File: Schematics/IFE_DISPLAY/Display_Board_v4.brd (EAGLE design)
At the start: 96.5 x 83.8 mm, 38 parts, among them J1 POWER_JACKPTH

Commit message: Display v4 - Routing
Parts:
- added R11, R4, R6: 23k, rcl:R0603
- added U$12: MC34063AD, Display_Custom:SMC
- J1: value POWER_JACKPTH -> 5.5x2.1mm Barrel; device SparkFun-Connectors:POWER_JACK_PTH -> SparkFun-Connectors:POWER_JACK_SMD
- moved J1 72.1 mm to (3.35, 68.6)
- moved U$7 33.0 mm to (8.89, 14.0)
- moved U$9 33.0 mm to (41.9, 14.0)
- moved R2 28.6 mm to (71.1, 60.9), turned to 180 degrees
- moved R3 28.6 mm to (71.1, 63.4), turned to 180 degrees
- moved C1 23.4 mm to (77.5, 61.0), turned to 90 degrees
- moved C2 20.1 mm to (64.8, 62.2), turned to 270 degrees
- moved U$11 18.2 mm to (59.7, 74.9), turned to 270 degrees
- moved U$10 15.3 mm to (73.7, 73.7), turned to 0 degrees
- moved R8 9.75 mm to (72.5, 40.6), turned to 90 degrees
- moved R9 9.68 mm to (72.3, 50.8), turned to 270 degrees
- moved C8 9.64 mm to (74.9, 40.6)
- moved C9 9.57 mm to (74.9, 50.8), turned to 270 degrees
- moved FUSE 9.16 mm to (85.1, 71.1), flipped to the bottom, turned to 90 degrees
- moved U$6 1.80 mm to (55.9, 49.5)
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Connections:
- net ~CS_CAN renamed !CS_CAN
- net ~INT_CAN renamed !INT_CAN
- new net !A_CS: ATMEGA328P.9, U$7.9
- new net !B_CS: ATMEGA328P.2, U$8.9
- new net !C_CS: ATMEGA328P.1, U$9.9
- new net A_0: U$1.12, U$7.3
- new net A_1: U$1.9, U$7.8
- new net A_2: U$1.8, U$7.5
- new net A_3: U$1.6, U$7.6
- new net A_A: U$1.11, U$7.11
- new net A_B: U$1.7, U$7.13
- new net A_C: U$1.4, U$7.17
- new net A_D: U$1.2, U$7.20
- new net A_DP: U$1.3, U$7.19
- new net A_E: U$1.1, U$7.18
- new net A_F: U$1.10, U$7.12
- new net A_G: U$1.5, U$7.14
- new net B_0: U$5.12, U$8.3
- new net B_1: U$5.9, U$8.8
- new net B_2: U$5.8, U$8.5
- new net B_3: U$5.6, U$8.6
- new net B_A: U$5.11, U$8.11
- new net B_B: U$5.7, U$8.13
- new net B_C: U$5.4, U$8.17
- new net B_D: U$5.2, U$8.20
- new net B_DP: U$5.3, U$8.19
- new net B_E: U$5.1, U$8.18
- new net B_F: U$5.10, U$8.12
- new net B_G: U$5.5, U$8.14
- new net C_0: U$6.12, U$9.3
- new net C_1: U$6.9, U$9.8
- new net C_2: U$6.8, U$9.5
- new net C_3: U$6.6, U$9.6
- new net C_A: U$6.11, U$9.11
- new net C_B: U$6.7, U$9.13
- new net C_C: U$6.4, U$9.17
- new net C_D: U$6.2, U$9.20
- new net C_DP: U$6.3, U$9.19
- new net C_E: U$6.1, U$9.18
- new net C_F: U$6.10, U$9.12
- new net C_G: U$6.5, U$9.14
- new net N$15: R6.1, U$8.15
- new net N$19: R11.1, U$9.15
- new net N$22: R4.1, U$7.15
- net +5V: now also R11.2, R4.2, R6.2, U$7.16, U$8.16, U$9.16
- net GND: now also J1.P$4, U$12.A, U$7.4, U$7.7, U$8.4, U$8.7, U$9.4, U$9.7; no longer J1.GNDBREAK
- net MISO: now also U$7.1, U$8.1, U$9.1
- net MOSI: now also U$7.2, U$8.2, U$9.2
- net N$8: now also U$12.C
- net PWR_IN_12: now also J1.VIN0; no longer J1.PWR
- net SCK: now also U$7.10, U$8.10, U$9.10
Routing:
- net PWR_IN_12: track 0.00 -> 134.3 mm
- net MISO: track 0.00 -> 61.8 mm, vias 0 -> 4
- net MOSI: track 0.00 -> 61.6 mm, vias 0 -> 4
- net CANL: track 0.00 -> 59.2 mm
- net CANH: track 0.00 -> 58.8 mm, vias 0 -> 1
- net GND: track 0.00 -> 52.2 mm
- net N$8: track 0.00 -> 39.7 mm
- net +5V: track 0.00 -> 35.6 mm, vias 0 -> 1
- net V+: track 0.00 -> 13.8 mm
- net 2515_OSC2: track 0.00 -> 12.3 mm
- net XTAL1: track 0.00 -> 11.5 mm
- net LED2: track 0.00 -> 9.45 mm
- net TXCAN: track 0.00 -> 8.70 mm
- net RESET: track 0.00 -> 8.25 mm
- net 2515_OSC1: track 0.00 -> 7.77 mm
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
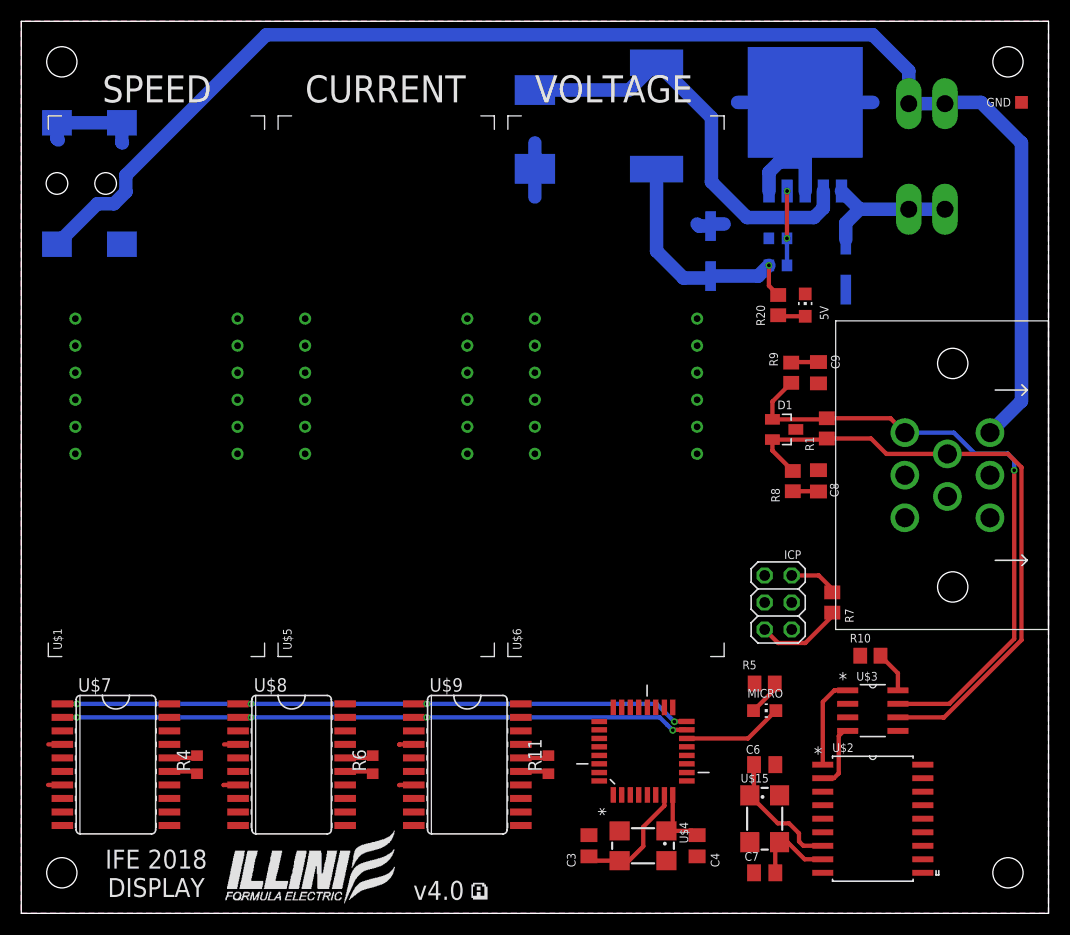
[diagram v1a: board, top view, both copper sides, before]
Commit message: Display v4 - ready to autoroute
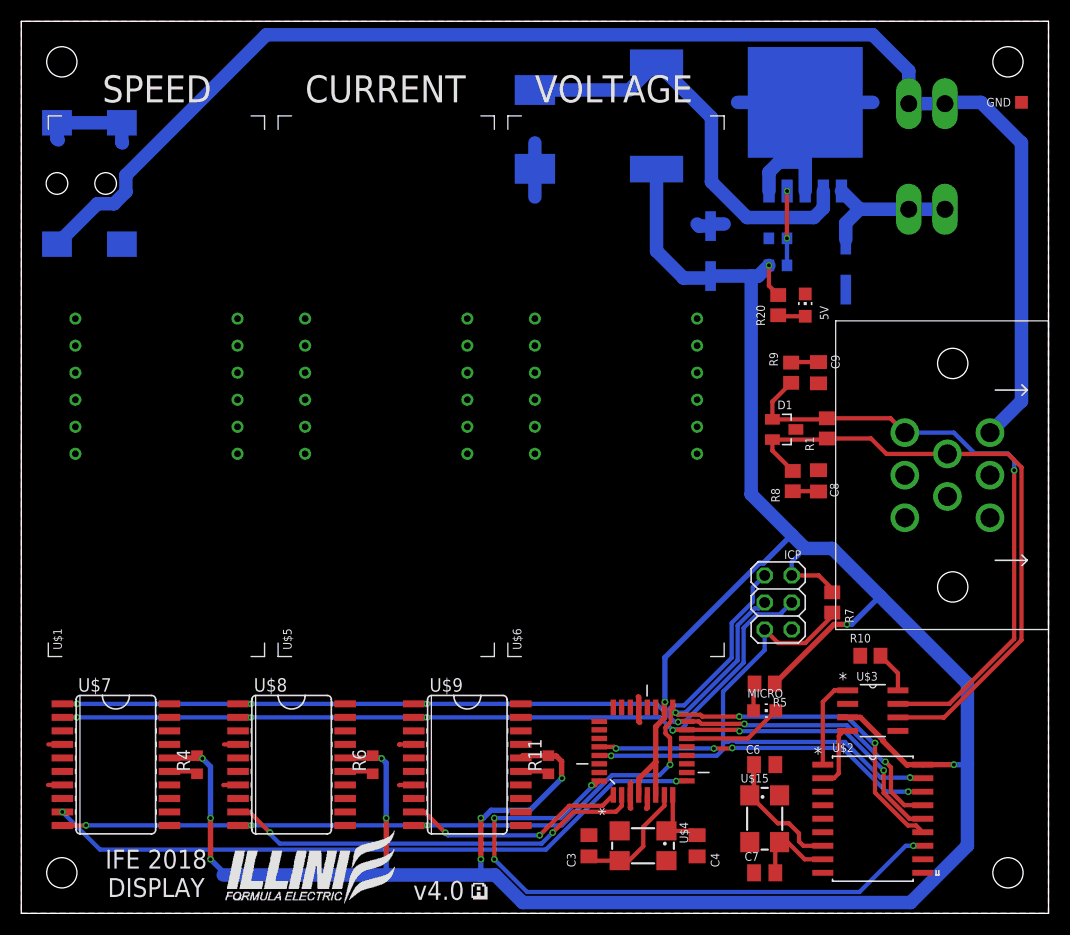
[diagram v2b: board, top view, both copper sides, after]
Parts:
- turned R5 to 0 degrees
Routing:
- net +5V: track 35.6 -> 277.8 mm, vias 1 -> 13
- net SCK: track 0.00 -> 113.6 mm, vias 0 -> 7
- net !A_CS: track 0.00 -> 62.8 mm, vias 0 -> 2
- net !INT_CAN: track 0.00 -> 58.6 mm, vias 0 -> 4
- net MOSI: track 61.6 -> 107.2 mm, vias 4 -> 6
- net RESET: track 8.25 -> 53.3 mm, vias 0 -> 2
- net MISO: track 61.8 -> 106.1 mm, vias 4 -> 6
- net !B_CS: track 0.00 -> 39.8 mm, vias 0 -> 2
- net !CS_CAN: track 0.00 -> 32.2 mm, vias 0 -> 4
- net !C_CS: track 0.00 -> 21.2 mm, vias 0 -> 2
- net GND: track 52.2 -> 58.4 mm
- net N$3: track 3.37 -> 2.58 mm

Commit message: Display v4 - autorouted
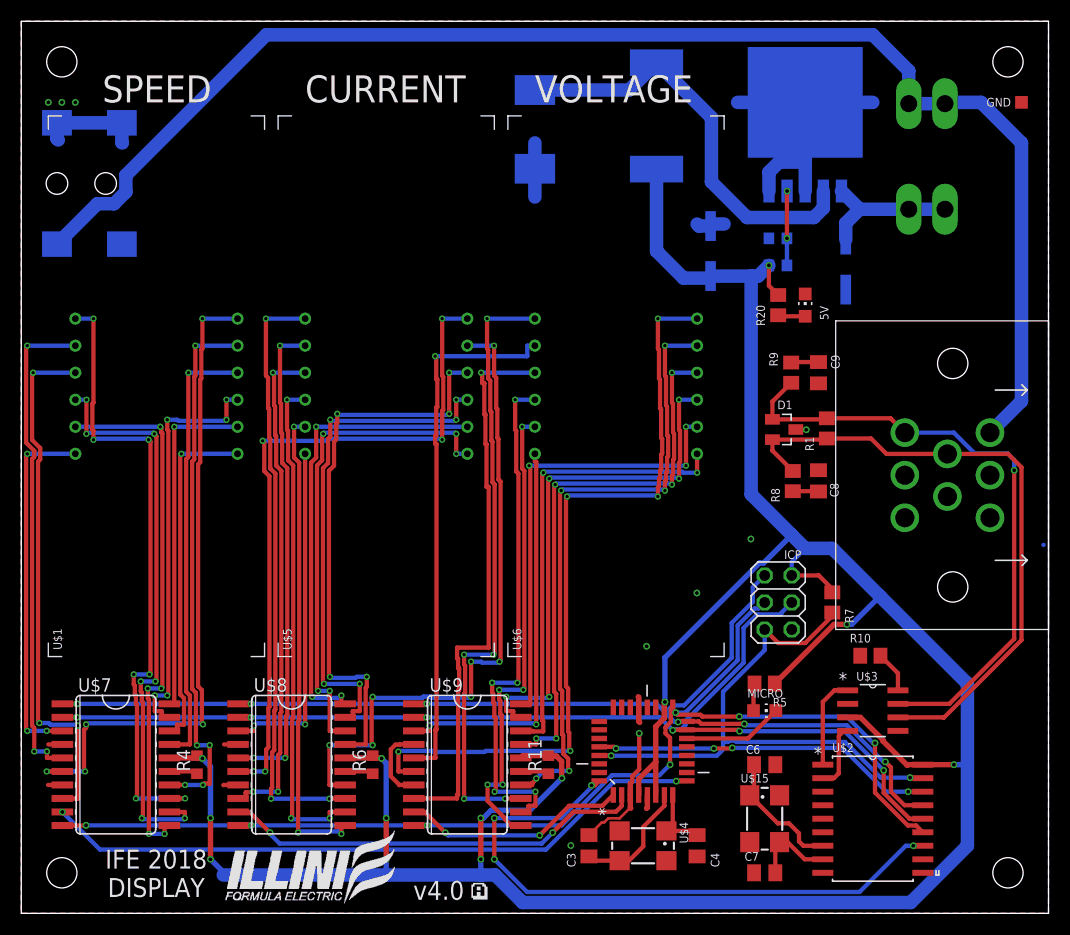
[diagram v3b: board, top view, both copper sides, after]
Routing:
- net C_3: track 0.00 -> 73.0 mm, vias 0 -> 5
- net B_3: track 0.00 -> 64.9 mm, vias 0 -> 5
- net A_3: track 0.00 -> 62.5 mm, vias 0 -> 5
- net B_G: track 0.00 -> 61.9 mm, vias 0 -> 7
- net A_B: track 0.00 -> 60.0 mm, vias 0 -> 7
- net C_G: track 0.00 -> 58.7 mm, vias 0 -> 5
- net C_B: track 0.00 -> 58.1 mm, vias 0 -> 5
- net B_B: track 0.00 -> 56.3 mm, vias 0 -> 3
- net A_F: track 0.00 -> 54.6 mm, vias 0 -> 7
- net B_C: track 0.00 -> 53.1 mm, vias 0 -> 5
- net C_1: track 0.00 -> 53.1 mm, vias 0 -> 1
- net C_C: track 0.00 -> 52.0 mm, vias 0 -> 5
- net C_2: track 0.00 -> 50.7 mm, vias 0 -> 1
- net A_G: track 0.00 -> 50.5 mm, vias 0 -> 5
- net A_A: track 0.00 -> 50.4 mm, vias 0 -> 5
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
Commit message: Display v4 - Adding FTDI for ease of programming
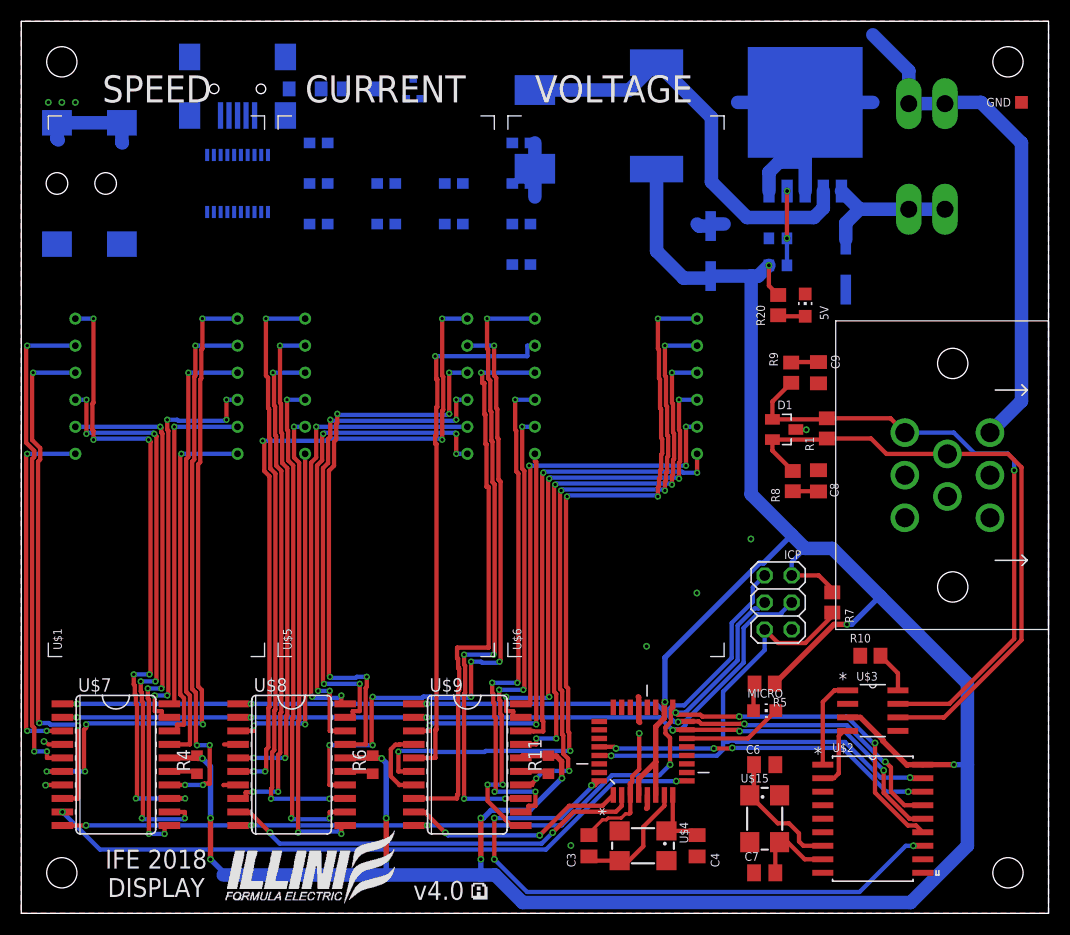
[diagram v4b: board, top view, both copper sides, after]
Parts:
- added C13, C5: 47pF, SparkFun-Capacitors:0603
- added C14: 0.1uF, SparkFun-Capacitors:0603
- added JP12: USB-MINIB-5PIN, SparkFun-Connectors:USB-MINIB
- added LED3: Red, SparkFun-LED:LED-1206
- added LED4: Yellow, SparkFun-LED:LED-1206
- added Q2: 2N7002PW, SparkFun-DiscreteSemi:SOT323
- added R12, R13, R14, R15: 1k, SparkFun-Resistors:0603
- added R16, R17: 27, SparkFun-Resistors:0603
- added R18, R19: 10k, SparkFun-Resistors:0603
- added U1: FT231XS, SparkFun-IC-Comms:SSOP20_L
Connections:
- removed net RXD: ATMEGA328P.30
- removed net TXD: ATMEGA328P.31
- new net 3.3V_F: C14.1, Q2.1, R18.2, U1.13, U1.14, U1.3
- new net D+: C5.1, JP12.D+, R17.1
- new net D-: C13.1, JP12.D-, R16.1
- new net DTR: Q2.3, R19.1
- new net FTDI_DTR: Q2.2, R18.1, U1.1
- new net N$1: LED3.A, R12.2
- new net N$10: LED4.A, R13.2
- new net N$2: R16.2, U1.12
- new net N$4: R17.2, U1.11
- new net RX-I: ATMEGA328P.30, R14.1
- new net RXD1: R15.2, U1.4
- new net RXLED: LED4.C, U1.17
- new net TX-O: ATMEGA328P.31, R15.1
- new net TXD1: R14.2, U1.20
- new net TXLED: LED3.C, U1.10
- net +5V: now also R12.1, R13.1, R19.2, U1.15
- net GND: now also C13.2, C14.2, C5.2, JP12.GND, JP12.MTN1, JP12.MTN2, JP12.MTN3, JP12.MTN4, U1.16, U1.6
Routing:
- net PWR_IN_12: track 134.3 -> 48.5 mm
- net GND: track 73.1 -> 73.9 mm, vias 9 -> 11

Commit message: v4 Ready to be printed
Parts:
- moved C5 25.4 mm to (21.6, 71.7), turned to 180 degrees
- moved R16 23.4 mm to (17.8, 69.8)
- moved C14 19.1 mm to (28.0, 66.8), turned to 180 degrees
- moved R15 19.1 mm to (27.9, 64.8)
- moved R19 16.6 mm to (33.0, 69.8), turned to 180 degrees
- moved R17 13.7 mm to (21.6, 69.8), turned to 180 degrees
- moved Q2 10.8 mm to (29.2, 69.8), turned to 90 degrees
- moved C13 10.1 mm to (17.8, 71.8)
- moved R12 9.16 mm to (35.6, 76.2)
- moved R14 5.87 mm to (27.9, 62.7)
- moved LED4 5.39 mm to (30.5, 73.7)
- moved R13 5.24 mm to (35.6, 73.7)
- moved R18 5.24 mm to (26.7, 69.8), turned to 270 degrees
- moved U1 5.08 mm to (20.3, 63.5), turned to 180 degrees
- moved LED3 1.80 mm to (30.5, 76.2)
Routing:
- net PWR_IN_12: track 48.5 -> 141.6 mm
- net TX-O: track 0.00 -> 70.2 mm, vias 0 -> 1
- net RX-I: track 0.00 -> 69.3 mm, vias 0 -> 3
- net +5V: track 277.8 -> 336.2 mm, vias 13 -> 17
- net RXLED: track 0.00 -> 23.1 mm, vias 0 -> 2
- net 3.3V_F: track 0.00 -> 20.9 mm, vias 0 -> 2
- net N$4: track 0.00 -> 19.9 mm
- net N$2: track 0.00 -> 15.4 mm
- net FTDI_DTR: track 0.00 -> 14.0 mm
- net TXD1: track 0.00 -> 13.4 mm
- net TXLED: track 0.00 -> 13.0 mm, vias 0 -> 2
- net RXD1: track 0.00 -> 9.13 mm
- net D-: track 0.00 -> 5.49 mm
- net D+: track 0.00 -> 5.29 mm
- net N$10: track 0.00 -> 2.73 mm
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
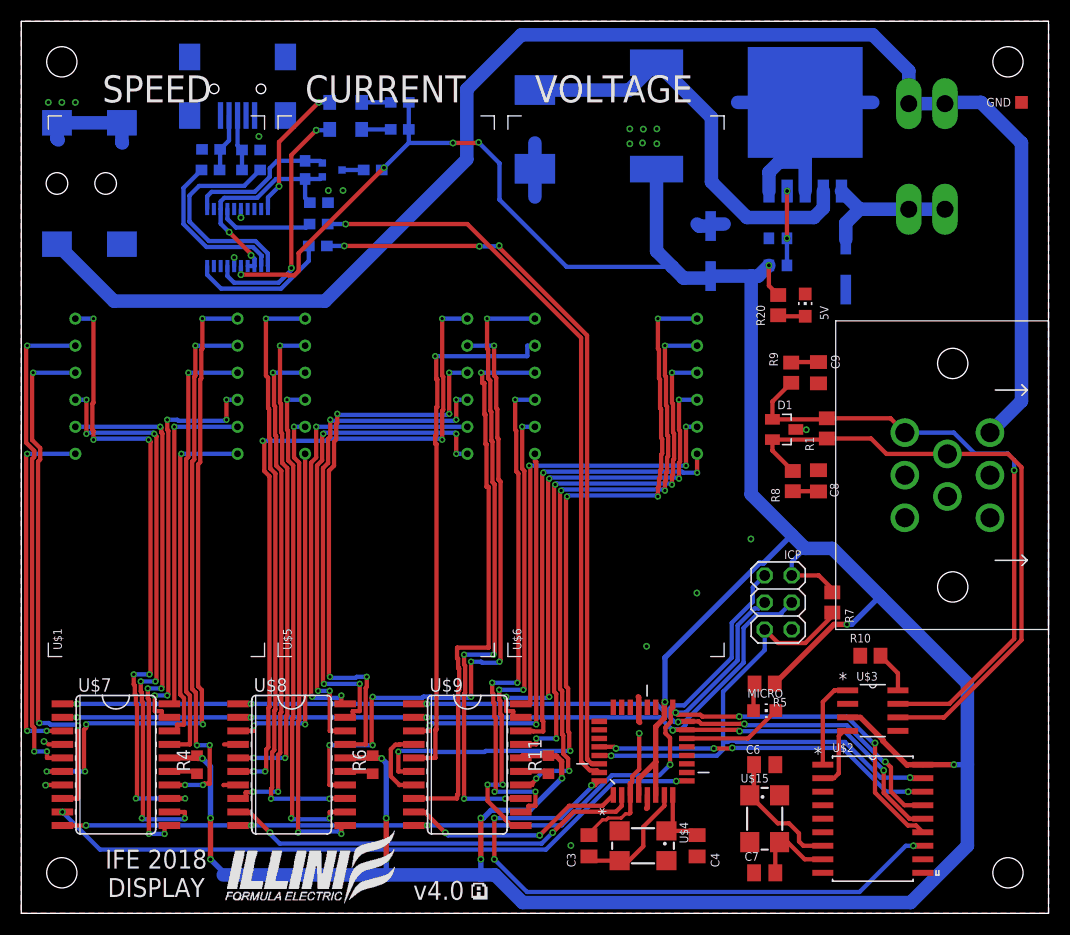
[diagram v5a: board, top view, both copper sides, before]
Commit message: added BOM
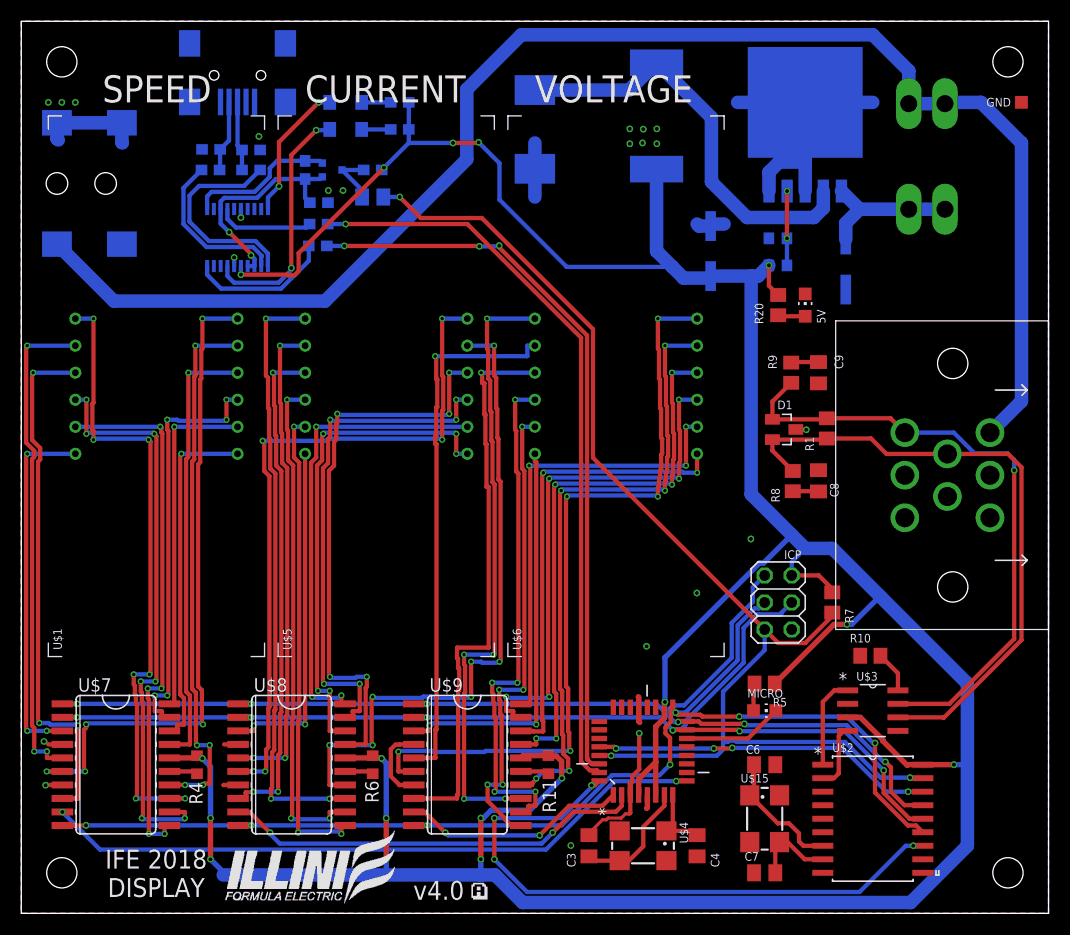
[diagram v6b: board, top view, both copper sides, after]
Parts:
- added C10: 0.1u, resistor:C0805K
- C1: value 680u -> 220u
- C2: value 220u -> 680u
- moved JP12 1.27 mm to (20.3, 78.7)
- renumbered LED3 to TX, LED4 to RX
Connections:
- net DTR: now also C10.2
- net RESET: now also C10.1
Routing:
- net RESET: track 53.3 -> 113.1 mm, vias 2 -> 3
- net DTR: track 2.04 -> 5.36 mm
- net D-: track 5.49 -> 6.76 mm
- net D+: track 5.29 -> 6.56 mm
